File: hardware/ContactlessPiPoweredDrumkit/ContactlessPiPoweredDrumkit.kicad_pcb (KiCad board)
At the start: 2 copper layers, 356.9 x 97.8 mm, 58 parts, among them J1 Raspberry_Pi_1_2_3, J2 Conn_01x06_Socket, J3 Conn_01x06_Socket, J4 Conn_01x06_Socket, J5 Conn_01x06_Socket, J6 Conn_01x06_Socket, J7 Conn_01x06_Socket, U1 VL53L4CD, U2 VL53L4CD, U3 VL53L4CD, U4 VL53L4CD, U5 VL53L4CD, U6 VL53L4CD, U7 SN74LVC1T45DCK

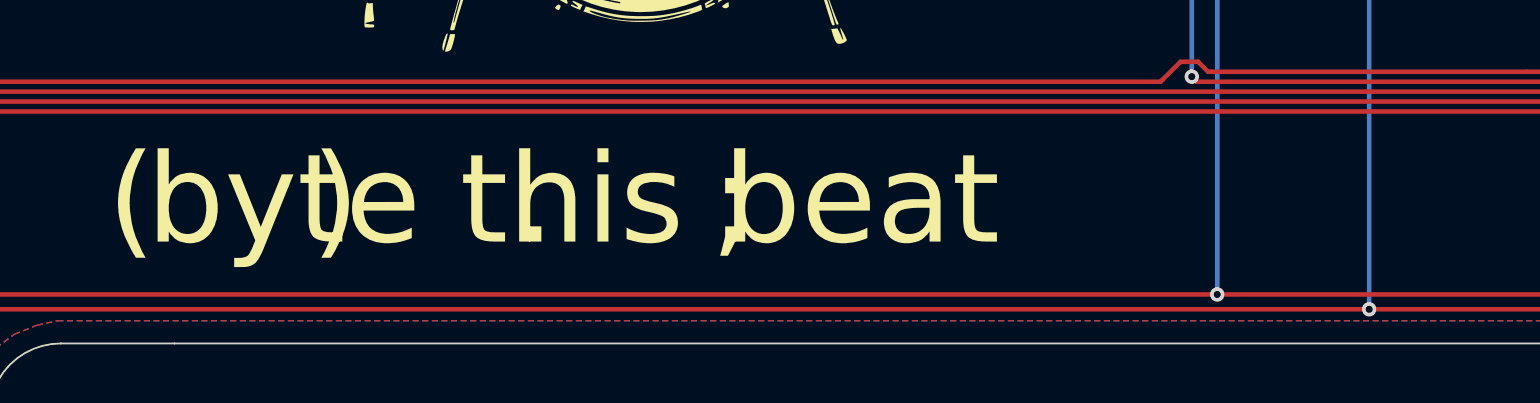
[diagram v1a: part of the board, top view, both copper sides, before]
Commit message: Create BOM
Create BOM
Modify Directory Structure
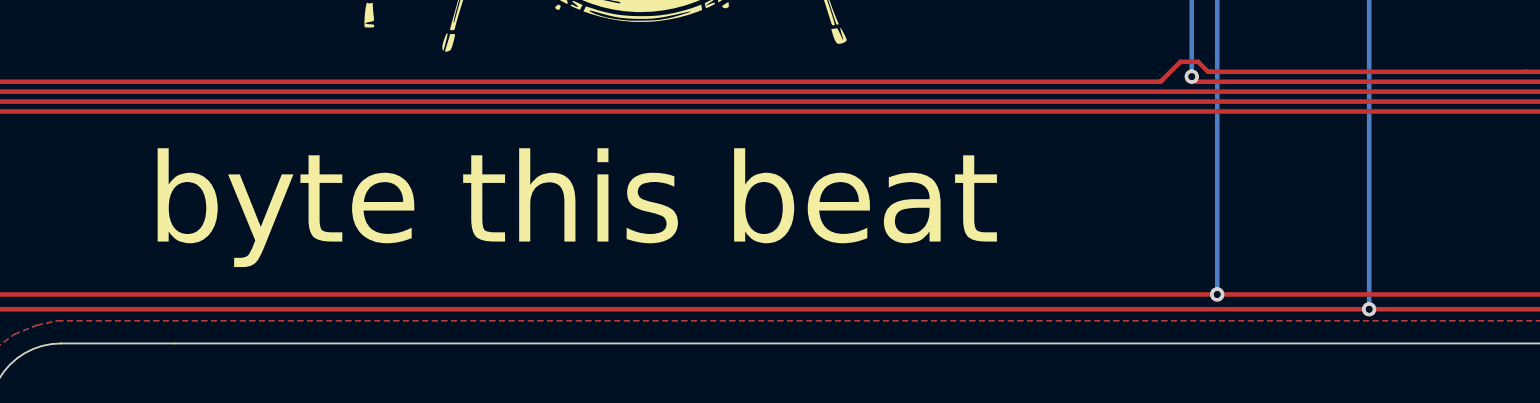
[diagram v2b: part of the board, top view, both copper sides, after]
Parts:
- added G***: LOGO, CustomArtwork:Drumstick, B.Cu at (343.4, 184.4)

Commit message: Reviewed PCB DRC
Reduced constraint size from .3mm to .25mm
Move pullup resistors slightly
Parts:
- moved G*** 0.79 mm to (104.0, 119.3)
- moved R12 0.09 mm to (318.5, 124.7)
- moved R9 0.09 mm to (322.9, 124.7)
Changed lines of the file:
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@@
       (sketchpadsonfab false)
       (subtractmaskfromsilk false)
-      (outputformat 4)
+      (outputformat 1)
       (mirror false)
-      (drillshape 2)
+      (drillshape 0)
       (scaleselection 1)
-      (outputdirectory "Assy/")
+      (outputdirectory "Gerbers/")
     )
   )
@@
   )
   (footprint "CustomArtwork:DrumsetKicad" (layer "F.Cu")
-    (at 103.251 119.38)
+    (at 104.0384 119.3292)
     (attr board_only exclude_from_pos_files exclude_from_bom)
     (fp_text reference "G***" (at 0 0) (layer "F.SilkS")
@@
   )
   (footprint "Resistor_SMD:R_0603_1608Metric" (layer "F.Cu")
-    (at 322.9102 124.7648 -90)
+    (at 322.9102 124.6754 -90)
     (descr "Resistor SMD 0603 (1608 Metric), square (rectangular) end terminal, IPC_7351 nominal, (Body size source: IPC-SM-782 page 72, https://www.pcb-3d.com/wordpress/wp-content/uploads/ipc-sm-782a_amendment_1_and_2.pdf), generated with kicad-footprint-generator")
     (tags "resistor")
@@
   )
   (footprint "Resistor_SMD:R_0603_1608Metric" (layer "F.Cu")
-    (at 318.4652 124.7648 -90)
+    (at 318.4652 124.6754 -90)
     (descr "Resistor SMD 0603 (1608 Metric), square (rectangular) end terminal, IPC_7351 nominal, (Body size source: IPC-SM-782 page 72, https://www.pcb-3d.com/wordpress/wp-content/uploads/ipc-sm-782a_amendment_1_and_2.pdf), generated with kicad-footprint-generator")
     (tags "resistor")
